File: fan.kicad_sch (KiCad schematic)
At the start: 15 parts, among them J6 Conn_01x04, J7 Conn_01x04, U10 EMC2101

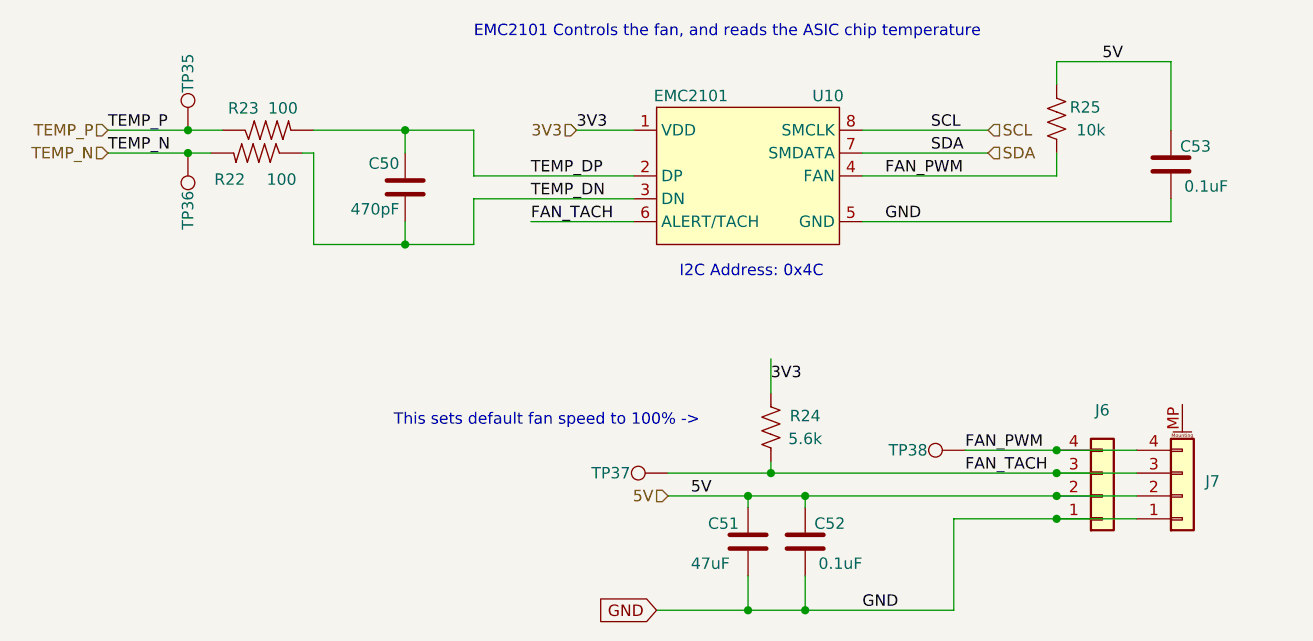
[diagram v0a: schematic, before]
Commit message: added files for model 605 Gamma Kit
Updated sizes for handsoldering kit, added onboard ethernet, cpu heatsink footprint, updated power supply
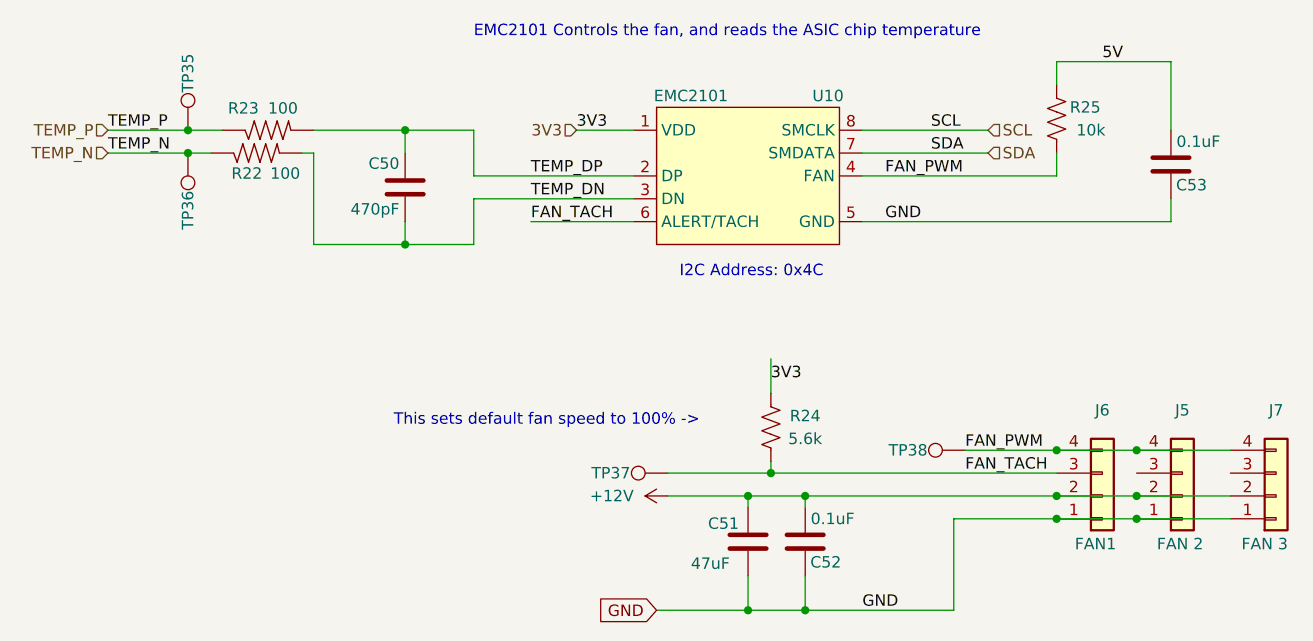
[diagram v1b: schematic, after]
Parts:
- removed J7: Conn_01x04, Connector_JST:JST_SH_BM04B-SRSS-TB_1x04-1MP_P1.00mm_Vertical, symbol Connector_Generic_MountingPin:Conn_01x04_MountingPin
- added J5, J7: Conn_01x04, bitaxe:470531000, symbol Connector_Generic:Conn_01x04
- C50: footprint Capacitor_SMD:C_0402_1005Metric -> Capacitor_SMD:C_0805_2012Metric_Pad1.18x1.45mm_HandSolder; DK 1276-1566-1-ND -> 4713-GMC21CG471K25NTCT-ND; PARTNO CL05B471KB5NNNC -> GMC21CG471K25NT
- C52, C53: footprint Capacitor_SMD:C_0402_1005Metric -> Capacitor_SMD:C_1206_3216Metric_Pad1.33x1.80mm_HandSolder; DK 1276-1234-1-ND -> 4713-GMC31CG104J50NTCT; PARTNO CL05A104KO5NNNC -> GMC31CG104J50NT
- R22, R23: footprint Resistor_SMD:R_0402_1005Metric -> Resistor_SMD:R_0805_2012Metric_Pad1.20x1.40mm_HandSolder; DK 311-100LRCT-ND -> 541-4374-1-ND; PARTNO RC0402FR-07100RL -> TNPW0805100RFEEA
- R24: footprint Resistor_SMD:R_0402_1005Metric -> Resistor_SMD:R_0805_2012Metric_Pad1.20x1.40mm_HandSolder; DK 13-RC0402FR-135K6LCT-ND -> 541-3221-1-ND; PARTNO RC0402FR-135K6L -> TNPW08055K60BEEA
- R25: footprint Resistor_SMD:R_0402_1005Metric -> Resistor_SMD:R_0805_2012Metric_Pad1.20x1.40mm_HandSolder; DK 311-10KJRCT-ND -> 541-3914-1-ND; PARTNO RC0402JR-0710KL -> TNPW080510K0DEEA
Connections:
- net 5V: no longer C51.1, C52.1, J6.2 (Pin_2)
- net FAN_PWM: now also J5.4 (Pin_4), J7.4 (Pin_4)
- net GND: now also J5.1 (Pin_1), J7.1 (Pin_1)
- net TEMP_DN: now also R22.2; no longer R22.1
- net TEMP_N: now also R22.1; no longer R22.2
- new net +12V: C51.1, C52.1, J5.2 (Pin_2), J6.2 (Pin_2), J7.2 (Pin_2)
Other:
- company: (none) -> Oconical
- title: bitaxeGamma -> bitaxeGamma 605 Kit
